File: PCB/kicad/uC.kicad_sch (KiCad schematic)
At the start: 21 parts, among them J12 M50-3530242, Y1 32MHZ

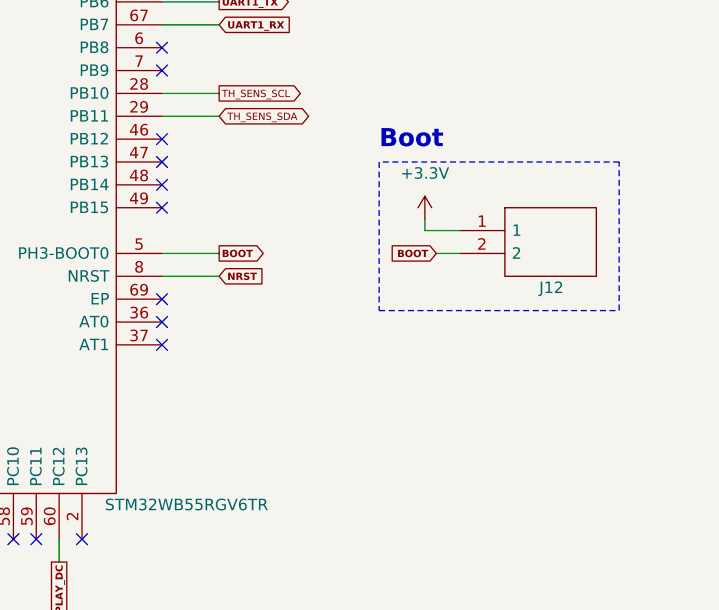
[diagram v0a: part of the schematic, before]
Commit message: Antenna chip replaced with antenna trace on PCB Switch replaced with button Added GND test point Added PD res on Boot pin Added NRST capacitor
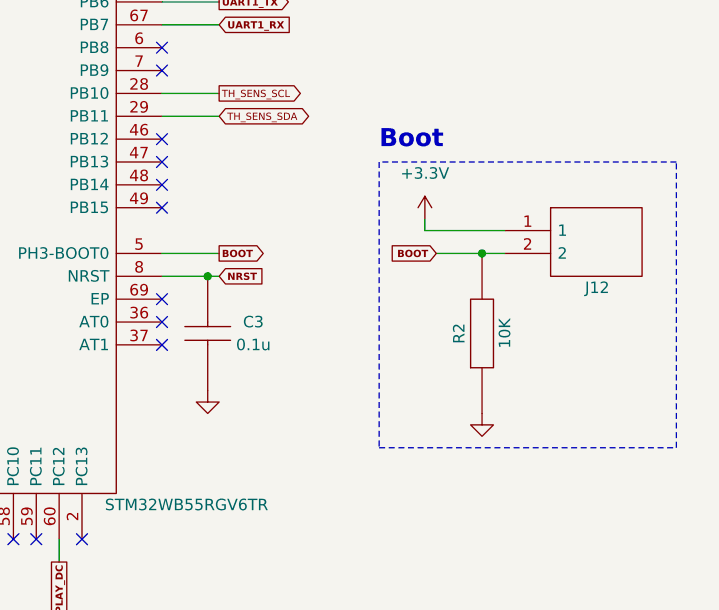
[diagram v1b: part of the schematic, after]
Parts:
- added C3: 0.1u, alecot:CAPC1005X55N, symbol alecot:GRM155R61H104KE19D
- added R2: 10K, alecot:RESC1608X55N, symbol alecot:ERJ-3EKF1002V
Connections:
- net BOOT: now also R2.2
- net GND: now also C3.2, R2.1
- net NRST: now also C3.1
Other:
- moved on the sheet: J12
